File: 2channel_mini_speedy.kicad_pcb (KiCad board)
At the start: 2 copper layers, 78.7 x 74.7 mm, 63 parts, among them J11 Molex MicroFit 3.0 43045-2400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, Q1 STP75NS04Z, Q2 STP75NS04Z, U1 TC4424EPA, U2 LM2940T, U3 Mega2560-PRO

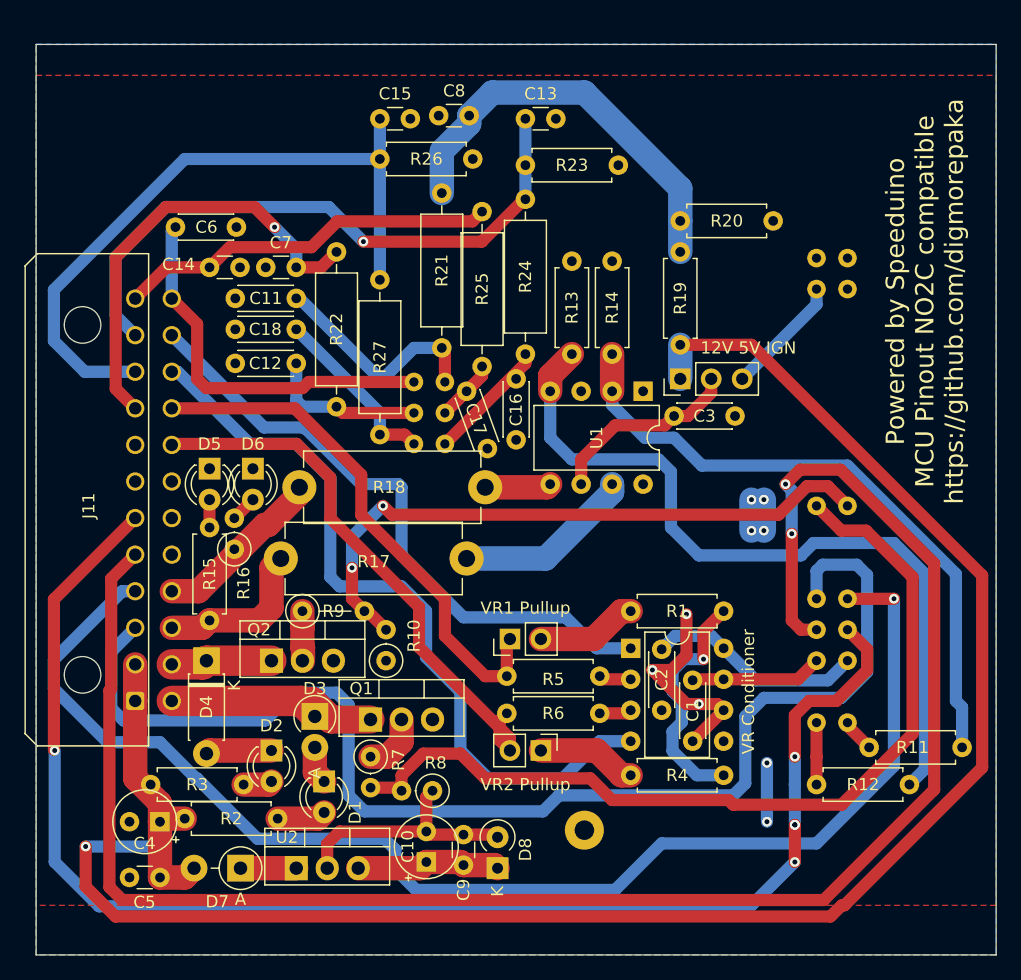
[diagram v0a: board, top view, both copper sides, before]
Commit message: fixed mosfet pinouts and ground plane
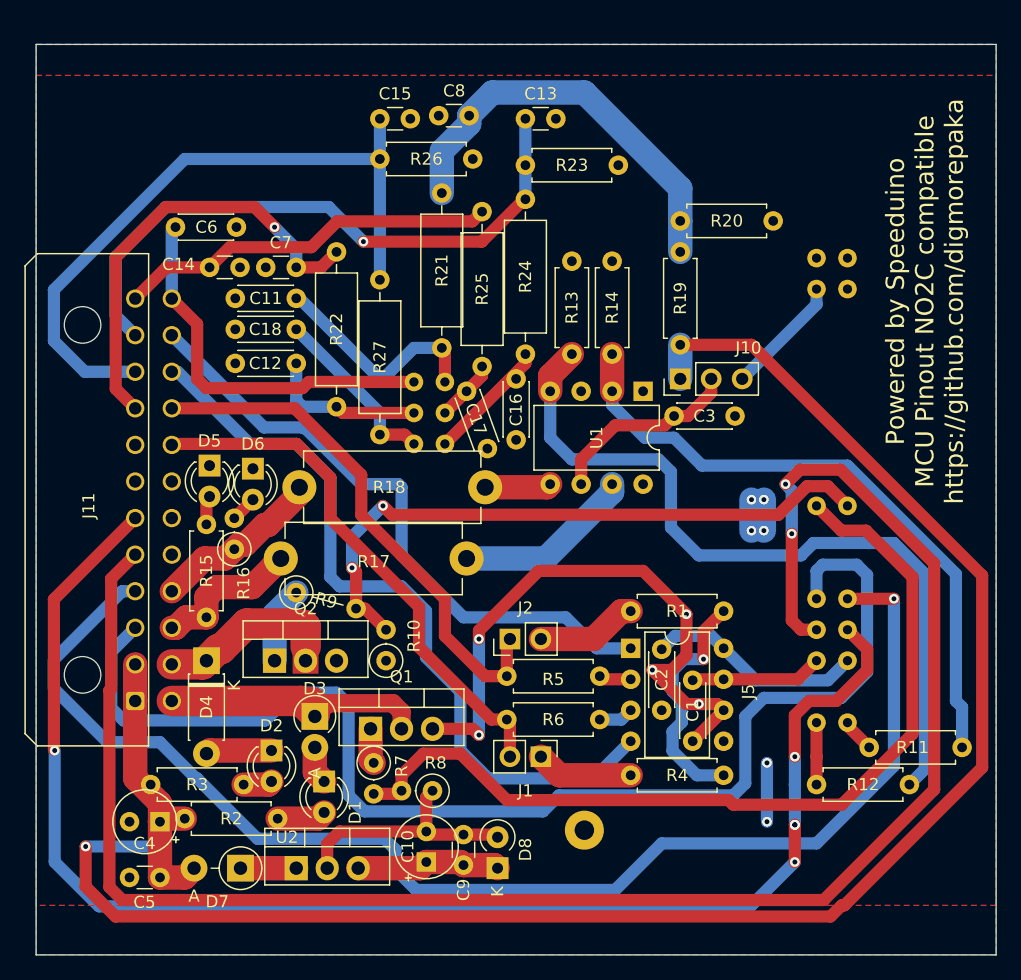
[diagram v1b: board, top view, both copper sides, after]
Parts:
- J1: renamed from VR2 Pullup
- J10: renamed from 12V 5V IGN
- J2: renamed from VR1 Pullup
- J5: renamed from VR Conditioner
- Q1, Q2: value STP75NS04Z -> STP75N04-TO220
- moved R9 1.61 mm to (47.5, 89.7), turned to 345 degrees
- moved Q1 0.76 mm to (53.6, 100.8)
- moved R7 0.57 mm to (53.8, 103.6)
- moved J1 0.51 mm to (67.6, 103.1)
- moved R6 0.51 mm to (72.4, 100.1)
- moved R15 0.36 mm to (40.1, 91.7)
- moved Q2 0.25 mm to (45.7, 95.2)
- moved D5 0.25 mm to (40.4, 79.2)
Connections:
- Q1 pad 1: INJ1 -> Net-(Q1-Pad1)
- Q1 pad 2: Net-(Q1-Pad2) -> INJ1
- Q2 pad 1: INJ2 -> Net-(Q2-Pad1)
- Q2 pad 2: Net-(Q2-Pad2) -> INJ2
- R7 pad 1: Net-(Q1-Pad2) -> Net-(Q1-Pad1)
- R9 pad 1: Net-(Q2-Pad2) -> Net-(Q2-Pad1)
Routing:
- net GND: track 39.0 -> 72.1 mm, vias 3 -> 5
- net Net-(Q2-Pad1): track 0.00 -> 6.32 mm
- net INJ2: track 8.29 -> 14.1 mm
- net Net-(Q1-Pad2): track 4.88 -> 0.00 mm
- net Net-(Q2-Pad2): track 4.08 -> 0.00 mm
- net INJ1: track 18.5 -> 22.3 mm
- net Net-(Q1-Pad1): track 0.00 -> 2.90 mm
- net VR2+: track 46.3 -> 43.9 mm
- net Net-(J5-Pad3): track 2.65 -> 3.21 mm
